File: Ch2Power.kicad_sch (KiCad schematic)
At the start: 10 parts, among them J201 Banana_Red, J202 Banana_Black

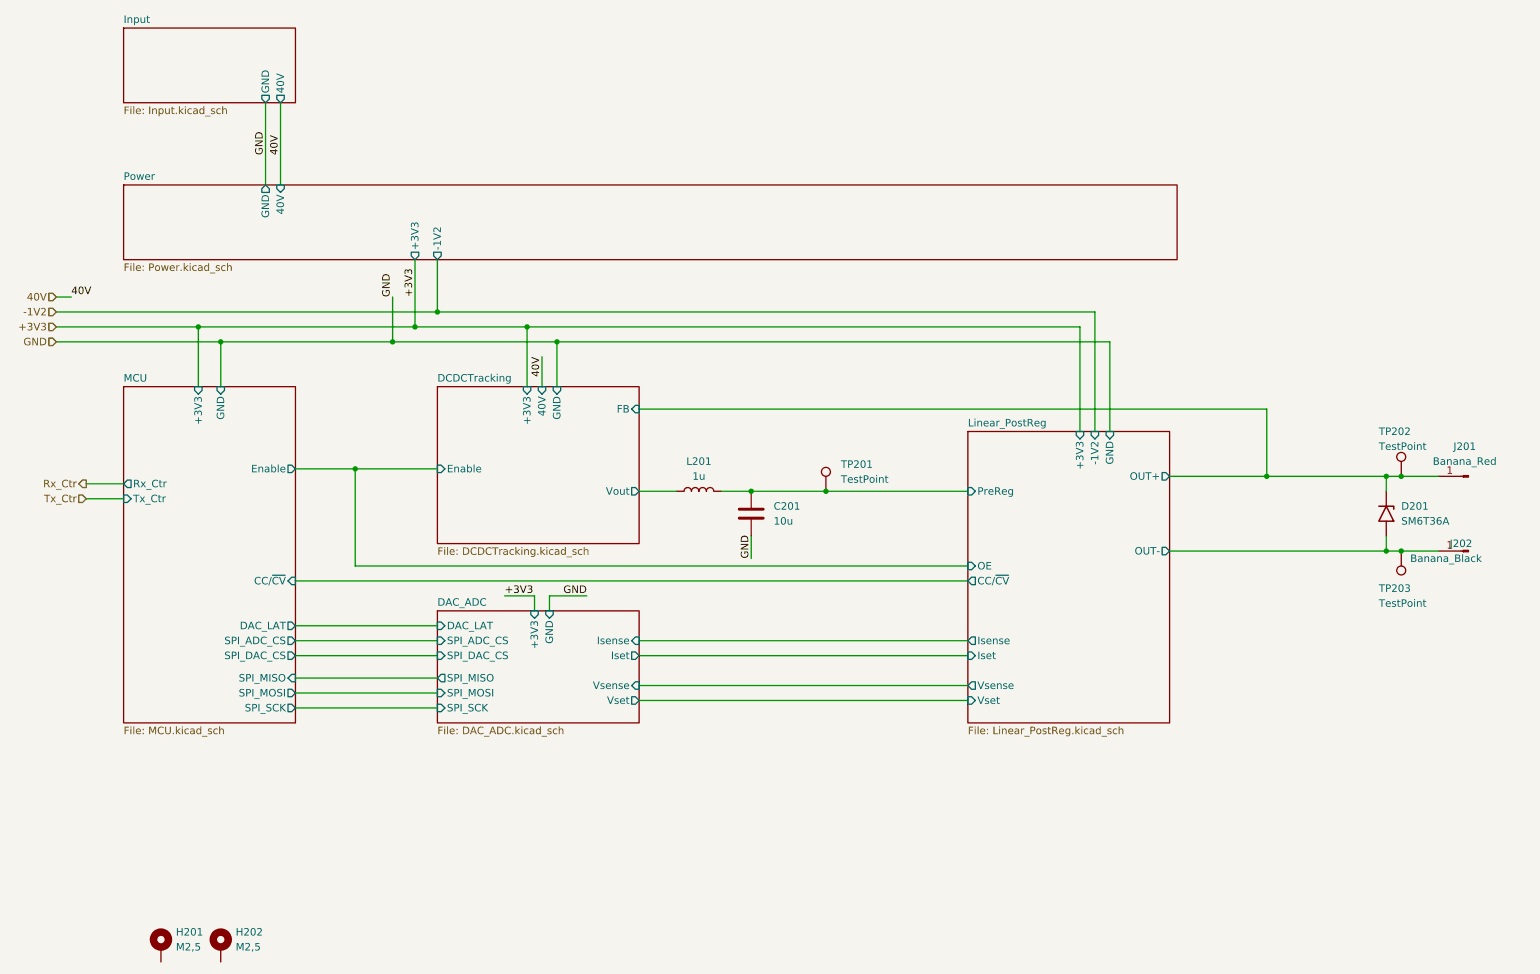
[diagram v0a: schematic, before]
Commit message: added Ch2 and removed global power flags
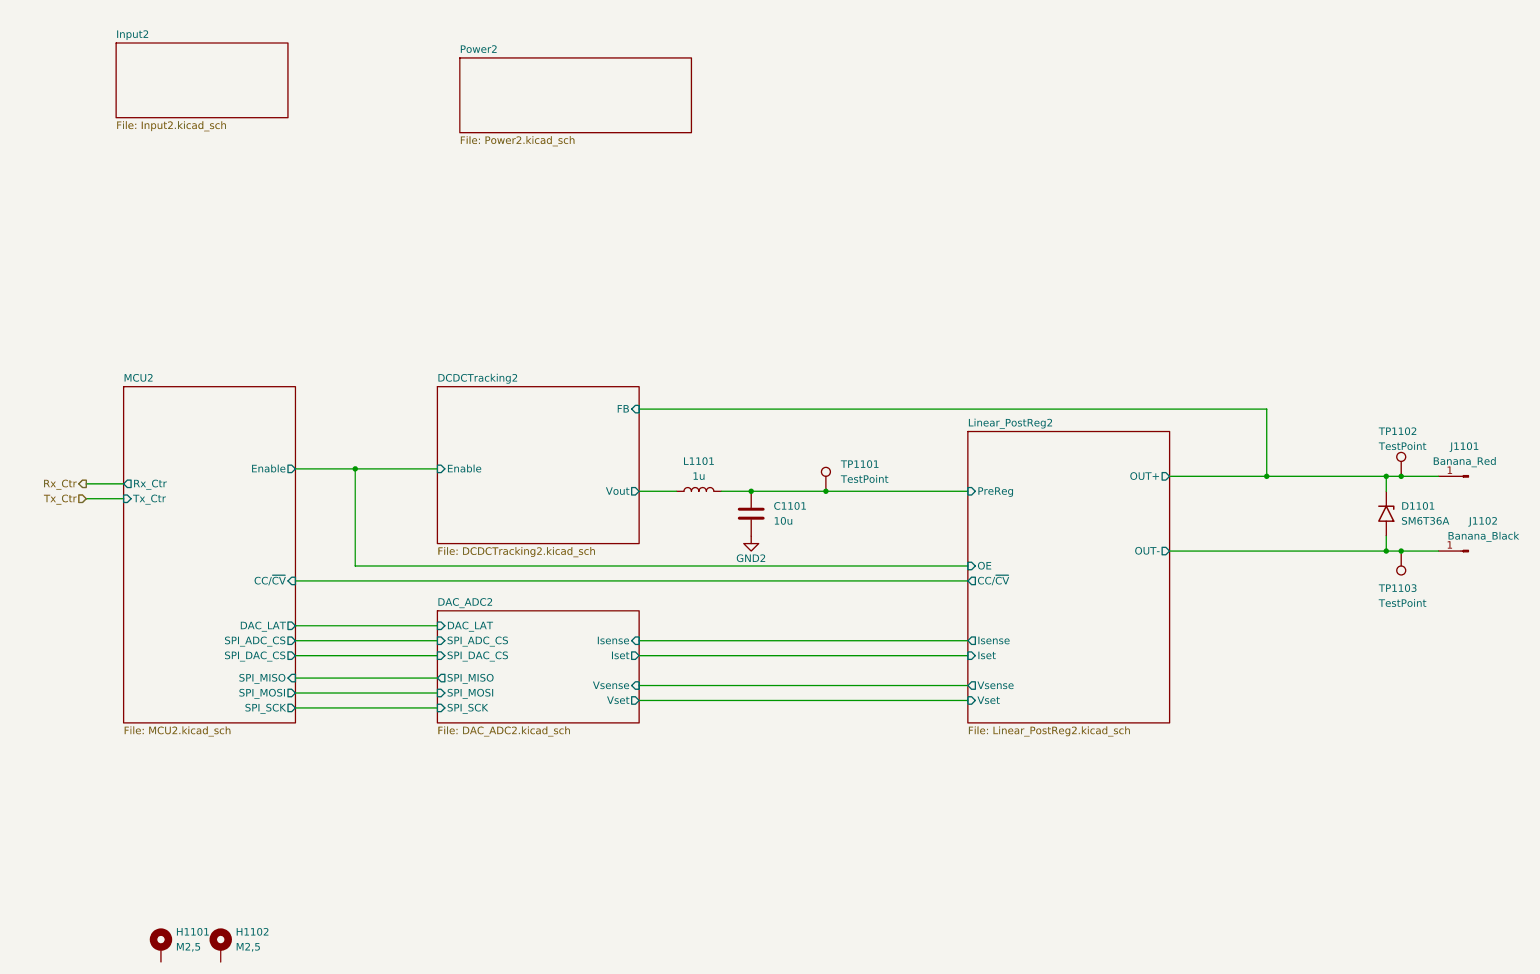
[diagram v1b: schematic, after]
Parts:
- removed C201: 10u, Capacitor_SMD:C_1206_3216Metric, symbol Device:C
- removed D201: SM6T36A, Diode_SMD:D_SMB, symbol Diode:SM6T36A
- removed H201, H202: M2,5, MountingHole:MountingHole_2.7mm_M2.5_DIN965_Pad, symbol Mechanical:MountingHole_Pad
- removed J201: Banana_Red, Connector:Banana_Cliff_FCR7350R_S16N-PC_Horizontal, symbol Connector:Conn_01x01_Pin
- removed J202: Banana_Black, Connector:Banana_Cliff_FCR7350B_S16N-PC_Horizontal, symbol Connector:Conn_01x01_Pin
- removed L201: 1u, Inductor_SMD:L_0805_2012Metric, symbol Device:L
- removed TP201, TP202, TP203: TestPoint, LibEigen:SMD Test Point PCWCTE, symbol Connector:TestPoint
- added C1101: 10u, Capacitor_SMD:C_1206_3216Metric, symbol Device:C
- added D1101: SM6T36A, Diode_SMD:D_SMB, symbol Diode:SM6T36A
- added H1101, H1102: M2,5, MountingHole:MountingHole_2.7mm_M2.5_DIN965_Pad, symbol Mechanical:MountingHole_Pad
- added J1101: Banana_Red, Connector:Banana_Cliff_FCR7350R_S16N-PC_Horizontal, symbol Connector:Conn_01x01_Pin
- added J1102: Banana_Black, Connector:Banana_Cliff_FCR7350B_S16N-PC_Horizontal, symbol Connector:Conn_01x01_Pin
- added L1101: 1u, Inductor_SMD:L_0805_2012Metric, symbol Device:L
- added TP1101, TP1102, TP1103: TestPoint, LibEigen:SMD Test Point PCWCTE, symbol Connector:TestPoint
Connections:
- new net DCDCTracking2/FB: D1101.1 (A1), J1101.1 (Pin_1), TP1102.1
- new net DCDCTracking2/Vout: L1101.1
- new net GND2: C1101.2
- new net Linear_PostReg2/OUT-: D1101.2 (A2), J1102.1 (Pin_1), TP1103.1
- new net Linear_PostReg2/PreReg: C1101.1, L1101.2, TP1101.1
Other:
- removed sheet DAC_ADC
- removed sheet DCDCTracking
- removed sheet Input
- removed sheet Linear_PostReg
- removed sheet MCU
- removed sheet Power
- added sheet DAC_ADC2 (DAC_ADC2.kicad_sch)
- added sheet DCDCTracking2 (DCDCTracking2.kicad_sch)
- added sheet Input2 (Input2.kicad_sch)
- added sheet Linear_PostReg2 (Linear_PostReg2.kicad_sch)
- added sheet MCU2 (MCU2.kicad_sch)
- added sheet Power2 (Power2.kicad_sch)
